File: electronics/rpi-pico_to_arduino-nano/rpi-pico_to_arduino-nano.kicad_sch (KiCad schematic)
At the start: 2 parts, among them U1 Pico

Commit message: add some connections and comments
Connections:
- net GPIO0: now reaches U1.1 (GPIO0)
- net GPIO0: now also A1.2 (D0/RX)
- net GPIO7: now reaches U1.10 (GPIO7)
- net GPIO7: now also A1.10 (D7)
- net GPIO8: now reaches U1.11 (GPIO8)
- net GPIO8: now also A1.11 (D8)
- net GPIO9: now reaches U1.12 (GPIO9)
- net GPIO9: now also A1.12 (D9)
- net GND: now reaches U1.13 (GND)
- net GND: now also A1.29 (GND), A1.4 (GND), U1.18 (GND), U1.23 (GND), U1.28 (GND), U1.3 (GND), U1.33 (AGND), U1.38 (GND), U1.42 (GND), U1.8 (GND)
- net GPIO10: now reaches U1.14 (GPIO10)
- net GPIO10: now also A1.13 (D10)
- net GPIO11: now reaches U1.15 (GPIO11)
- net GPIO11: now also A1.14 (D11)
- net GPIO12: now reaches U1.16 (GPIO12)
- net GPIO12: now also A1.15 (D12)
- net GPIO13: now reaches U1.17 (GPIO13)
- net GPIO13: now also A1.16 (D13)
- net GPIO14: now reaches U1.19 (GPIO14)
- net GPIO1: now reaches U1.2 (GPIO1)
- net GPIO1: now also A1.1 (D1/TX)
- net GPIO15: now reaches U1.20 (GPIO15)
- net GPIO16: now reaches U1.21 (GPIO16)
- net GPIO17: now reaches U1.22 (GPIO17)
- net GPIO18: now reaches U1.24 (GPIO18)
- net GPIO19: now reaches U1.25 (GPIO19)
- net GPIO20: now reaches U1.26 (GPIO20)
- net GPIO21: now reaches U1.27 (GPIO21)
- net GPIO22: now reaches U1.29 (GPIO22)
- net RUN: now reaches U1.30 (RUN)
- net GPIO26_ADC0: now reaches U1.31 (GPIO26_ADC0)
- net GPIO26_ADC0: now also A1.19 (A0), A1.21 (A2)
- net GPIO27_ADC1: now reaches U1.32 (GPIO27_ADC1)
- net GPIO27_ADC1: now also A1.20 (A1)
- net GPIO28_ADC2: now reaches U1.34 (GPIO28_ADC2)
- net ADC_VREF: now reaches U1.35 (ADC_VREF)
- net 3V3: now reaches U1.36 (3V3)
- net 3V3_EN: now reaches U1.37 (3V3_EN)
- net VSYS: now reaches U1.39 (VSYS)
- net GPIO2: now reaches U1.4 (GPIO2)
- net GPIO2: now also A1.5 (D2)
- net VBUS: now reaches U1.40 (VBUS)
- net SWCLK: now reaches U1.41 (SWCLK)
- net SWDIO: now reaches U1.43 (SWDIO)
- net GPIO3: now reaches U1.5 (GPIO3)
- net GPIO3: now also A1.6 (D3)
- net GPIO4: now reaches U1.6 (GPIO4)
- net GPIO4: now also A1.7 (D4)
- net GPIO5: now reaches U1.7 (GPIO5)
- net GPIO5: now also A1.8 (D5)
- net GPIO6: now reaches U1.9 (GPIO6)
- net GPIO6: now also A1.9 (D6)
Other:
- note added: "!!! TODO: check if connections at the Arduino make sense => also according to relay print!!!! => Pico Relay B will not work currently!!!! It should work out of the box (without modifications) !!!"
- note added: "Pico Relay B pinout"
- moved on the sheet: A1, U1

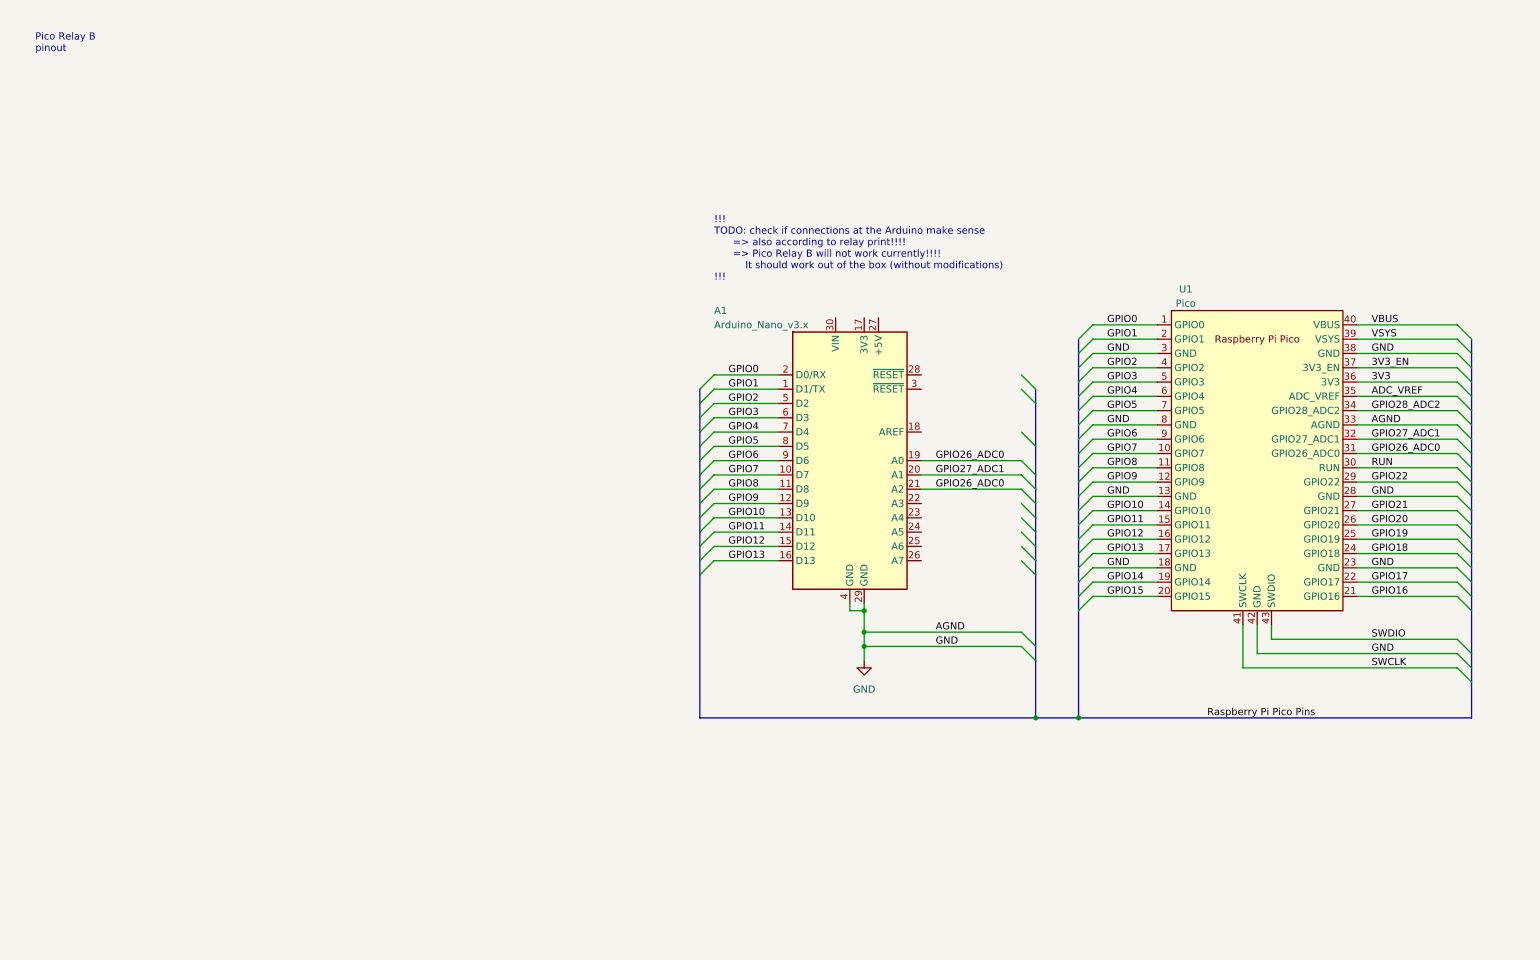
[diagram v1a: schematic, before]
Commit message: add connection matrix
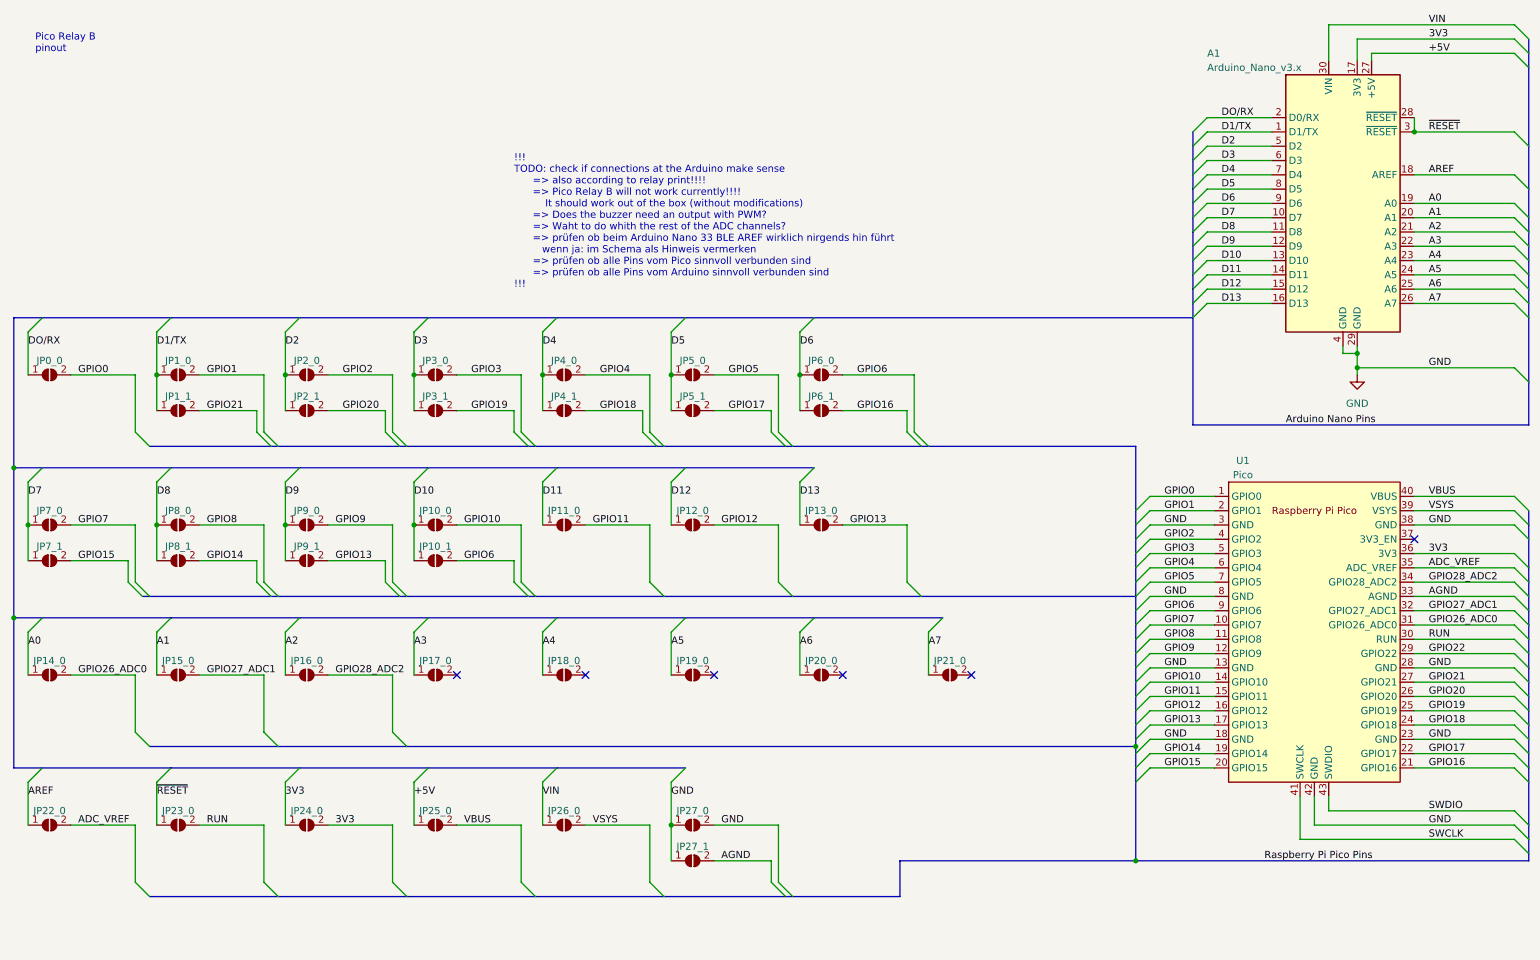
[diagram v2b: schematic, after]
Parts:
- added JP0_0, JP10_0, JP10_1, JP11_0, JP12_0, JP13_0, JP14_0, JP15_0, JP16_0, JP17_0, JP18_0, JP19_0, JP1_0, JP1_1, JP20_0, JP21_0, JP22_0, JP23_0, JP24_0, JP25_0, JP26_0, JP27_0, JP27_1, JP2_0, JP2_1, JP3_0, JP3_1, JP4_0, JP4_1, JP5_0, JP5_1, JP6_0, JP6_1, JP7_0, JP7_1, JP8_0, JP8_1, JP9_0, JP9_1: SolderJumper_2_Open, Jumper:SolderJumper-2_P1.3mm_Open_RoundedPad1.0x1.5mm, symbol Jumper:SolderJumper_2_Open
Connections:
- net 3V3: now also A1.17 (3V3), JP24_0.1 (A), JP24_0.2 (B)
- net ADC_VREF: now also JP22_0.2 (B)
- net GND: now also JP27_0.1 (A), JP27_0.2 (B), JP27_1.1 (A); no longer U1.33 (AGND)
- net GPIO0: now also JP0_0.2 (B); no longer A1.2 (D0/RX)
- net GPIO1: now also JP1_0.2 (B); no longer A1.1 (D1/TX)
- net GPIO10: now also JP10_0.2 (B); no longer A1.13 (D10)
- net GPIO11: now also JP11_0.2 (B); no longer A1.14 (D11)
- net GPIO12: now also JP12_0.2 (B); no longer A1.15 (D12)
- net GPIO13: now also JP13_0.2 (B), JP9_1.2 (B); no longer A1.16 (D13)
- net GPIO14: now also JP8_1.2 (B)
- net GPIO15: now also JP7_1.2 (B)
- net GPIO16: now also JP6_1.2 (B)
- net GPIO17: now also JP5_1.2 (B)
- net GPIO18: now also JP4_1.2 (B)
- net GPIO19: now also JP3_1.2 (B)
- net GPIO2: now also JP2_0.2 (B); no longer A1.5 (D2)
- net GPIO20: now also JP2_1.2 (B)
- net GPIO21: now also JP1_1.2 (B)
- net GPIO26_ADC0: now also JP14_0.2 (B); no longer A1.19 (A0), A1.21 (A2)
- net GPIO27_ADC1: now also JP15_0.2 (B); no longer A1.20 (A1)
- net GPIO28_ADC2: now also JP16_0.2 (B)
- net GPIO3: now also JP3_0.2 (B); no longer A1.6 (D3)
- net GPIO4: now also JP4_0.2 (B); no longer A1.7 (D4)
- net GPIO5: now also JP5_0.2 (B); no longer A1.8 (D5)
- net GPIO6: now also JP10_1.2 (B), JP6_0.2 (B); no longer A1.9 (D6)
- net GPIO7: now also JP7_0.2 (B); no longer A1.10 (D7)
- net GPIO8: now also JP8_0.2 (B); no longer A1.11 (D8)
- net GPIO9: now also JP9_0.2 (B); no longer A1.12 (D9)
- net RUN: now also JP23_0.2 (B)
- net VBUS: now also JP25_0.2 (B)
- net VSYS: now also JP26_0.2 (B)
- net AREF: now reaches A1.18 (AREF)
- net AREF: now also JP22_0.1 (A)
- net A3: now reaches A1.22 (A3)
- net A3: now also JP17_0.1 (A)
- net A4: now reaches A1.23 (A4)
- net A4: now also JP18_0.1 (A)
- net A5: now reaches A1.24 (A5)
- net A5: now also JP19_0.1 (A)
- net A6: now reaches A1.25 (A6)
- net A6: now also JP20_0.1 (A)
- net A7: now reaches A1.26 (A7)
- net A7: now also JP21_0.1 (A)
- net +5V: now reaches A1.27 (+5V)
- net +5V: now also JP25_0.1 (A)
- net ~{RESET}: now reaches A1.28 (~{RESET})
- net ~{RESET}: now also A1.3 (~{RESET}), JP23_0.1 (A)
- net VIN: now reaches A1.30 (VIN)
- net VIN: now also JP26_0.1 (A)
- net 3V3_EN: no longer names the net of U1.37 (3V3_EN)
- new net A0: A1.19 (A0), JP14_0.1 (A)
- new net A1: A1.20 (A1), JP15_0.1 (A)
- new net A2: A1.21 (A2), JP16_0.1 (A)
- new net AGND: JP27_1.2 (B), U1.33 (AGND)
- new net D10: A1.13 (D10), JP10_0.1 (A), JP10_1.1 (A)
- new net D11: A1.14 (D11), JP11_0.1 (A)
- new net D12: A1.15 (D12), JP12_0.1 (A)
- new net D13: A1.16 (D13), JP13_0.1 (A)
- new net D1/TX: A1.1 (D1/TX), JP1_0.1 (A), JP1_1.1 (A)
- new net D2: A1.5 (D2), JP2_0.1 (A), JP2_1.1 (A)
- new net D3: A1.6 (D3), JP3_0.1 (A), JP3_1.1 (A)
- new net D4: A1.7 (D4), JP4_0.1 (A), JP4_1.1 (A)
- new net D5: A1.8 (D5), JP5_0.1 (A), JP5_1.1 (A)
- new net D6: A1.9 (D6), JP6_0.1 (A), JP6_1.1 (A)
- new net D7: A1.10 (D7), JP7_0.1 (A), JP7_1.1 (A)
- new net D8: A1.11 (D8), JP8_0.1 (A), JP8_1.1 (A)
- new net D9: A1.12 (D9), JP9_0.1 (A), JP9_1.1 (A)
- new net DO/RX: A1.2 (D0/RX), JP0_0.1 (A)
- no-connect marks 0 -> 6
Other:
- note added: "!!! TODO: check if connections at the Arduino make sense => also according to relay print!!!! => Pico Relay B will not work currently!!!! It should work out of the box (without modifications) => Does the buzzer need an output with PWM? => Waht to do whith the rest of the ADC channels? => prüfen ob beim Arduino Nano 33 BLE AREF wirklich nirgends hin führt wenn ja: im Schema als Hinweis vermerken =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"
- note removed: "!!! TODO: check if connections at the Arduino make sense => also according to relay print!!!! => Pico Relay B will not work currently!!!! It should work out of the box (without modifications) !!!"
- moved on the sheet: A1, U1

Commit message: place components on pcb
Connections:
- net 3V3: no longer JP24_0.2 (B), U1.36 (3V3)
- net GND: no longer JP27_0.2 (B), U1.13 (GND), U1.18 (GND), U1.23 (GND), U1.28 (GND), U1.3 (GND), U1.38 (GND), U1.42 (GND), U1.8 (GND)
- net GPIO22: now also JP17_0.2 (B)
- net SWCLK: no longer names the net of U1.41 (SWCLK)
- net SWDIO: no longer names the net of U1.43 (SWDIO)
- new net 3V3_pico: JP24_0.2 (B), U1.36 (3V3)
- new net GND_pico: JP27_0.2 (B), U1.13 (GND), U1.18 (GND), U1.23 (GND), U1.28 (GND), U1.3 (GND), U1.38 (GND), U1.42 (GND), U1.8 (GND)
- no-connect marks 6 -> 7
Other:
- note added: "!!! TODO: check if connections at the Arduino make sense (done)=> Does the buzzer need an output with PWM? => yes and done => how does the rgb led work and with only one pin? => prüfen ob beim Arduino Nano 33 BLE AREF wirklich nirgends hin führt wenn ja: im Schema als Hinweis vermerken => entscheiden welche Lötjumper per default geschlossen sein sollen !!! Delete this text before when done"
- note removed: "!!! TODO: check if connections at the Arduino make sense => also according to relay print!!!! => Pico Relay B will not work currently!!!! It should work out of the box (without modifications) => Does the buzzer need an output with PWM? => Waht to do whith the rest of the ADC channels? => prüfen ob beim Arduino Nano 33 BLE AREF wirklich nirgends hin führt wenn ja: im Schema als Hinweis vermerken =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"
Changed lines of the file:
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@@
   (junction (at 16.51 104.14) (diameter 0) (color 0 0 0 0)
   )
+  (no_connect (at 262.89 106.68))
+  (no_connect (at 247.65 152.4))
+  (no_connect (at 242.57 152.4))
   (no_connect (at 184.15 130.81))
   (no_connect (at 161.29 130.81))
-  (no_connect (at 115.57 130.81))
-  (no_connect (at 92.71 130.81))
   (no_connect (at 138.43 130.81))
-  (no_connect (at 262.89 106.68))
+  (no_connect (at 115.57 130.81))
   (bus_entry (at 80.01 114.3) (size 2.54 2.54)
     (stroke (width 0) (type default) (color 0 0 0 0))
@@
     (stroke (width 0) (type default) (color 0 0 0 0))
   )
+  (bus_entry (at 104.14 140.97) (size 2.54 2.54)
+    (stroke (width 0) (type default) (color 0 0 0 0))
+  )
   (bus_entry (at 87.63 147.32) (size -2.54 2.54)
     (stroke (width 0) (type default) (color 0 0 0 0))
@@
     (stroke (width 0) (type default) (color 0 0 0 0))
   )
-  (bus_entry (at 283.21 157.48) (size -2.54 -2.54)
-    (stroke (width 0) (type default) (color 0 0 0 0))
-  )
-  (bus_entry (at 280.67 160.02) (size 2.54 2.54)
-    (stroke (width 0) (type default) (color 0 0 0 0))
-  )
   (bus_entry (at 133.35 67.31) (size -2.54 2.54)
     (stroke (width 0) (type default) (color 0 0 0 0))
@@
     (stroke (width 0) (type default) (color 0 0 0 0))
   )
-  (wire (pts (xy 242.57 152.4) (xy 242.57 160.02))
-    (stroke (width 0) (type default) (color 0 0 0 0))
-  )
   (wire (pts (xy 215.9 111.76) (xy 227.33 111.76))
     (stroke (width 0) (type default) (color 0 0 0 0))
@@
     (stroke (width 0) (type default) (color 0 0 0 0))
   )
-  (bus (pts (xy 283.21 162.56) (xy 283.21 163.83))
+  (bus (pts (xy 283.21 160.02) (xy 283.21 163.83))
     (stroke (width 0) (type default) (color 0 0 0 0))
   )
@@
     (stroke (width 0) (type default) (color 0 0 0 0))
   )
-  (bus (pts (xy 283.21 149.86) (xy 283.21 157.48))
+  (bus (pts (xy 283.21 149.86) (xy 283.21 160.02))
     (stroke (width 0) (type default) (color 0 0 0 0))
   )
@@
     (stroke (width 0) (type default) (color 0 0 0 0))
   )
+  (wire (pts (xy 104.14 130.81) (xy 104.14 140.97))
+    (stroke (width 0) (type default) (color 0 0 0 0))
+  )
   (wire (pts (xy 92.71 157.48) (xy 104.14 157.48))
     (stroke (width 0) (type default) (color 0 0 0 0))
@@
     (stroke (width 0) (type default) (color 0 0 0 0))
   )
-  (wire (pts (xy 247.65 152.4) (xy 247.65 154.94))
-    (stroke (width 0) (type default) (color 0 0 0 0))
-  )
   (wire (pts (xy 262.89 121.92) (xy 280.67 121.92))
     (stroke (width 0) (type default) (color 0 0 0 0))
@@
     (stroke (width 0) (type default) (color 0 0 0 0))
   )
+  (bus (pts (xy 106.68 143.51) (xy 213.36 143.51))
+    (stroke (width 0) (type default) (color 0 0 0 0))
+  )
   (bus (pts (xy 213.36 119.38) (xy 213.36 121.92))
     (stroke (width 0) (type default) (color 0 0 0 0))
@@
     (stroke (width 0) (type default) (color 0 0 0 0))
   )
+  (wire (pts (xy 92.71 130.81) (xy 104.14 130.81))
+    (stroke (width 0) (type default) (color 0 0 0 0))
+  )
   (wire (pts (xy 58.42 77.47) (xy 58.42 87.63))
     (stroke (width 0) (type default) (color 0 0 0 0))
@@
     (stroke (width 0) (type default) (color 0 0 0 0))
   )
-  (bus (pts (xy 283.21 157.48) (xy 283.21 160.02))
-    (stroke (width 0) (type default) (color 0 0 0 0))
-  )
   (wire (pts (xy 226.06 34.29) (xy 237.49 34.29))
     (stroke (width 0) (type default) (color 0 0 0 0))
@@
     (stroke (width 0) (type default) (color 0 0 0 0))
   )
-  (bus (pts (xy 83.82 143.51) (xy 213.36 143.51))
+  (bus (pts (xy 83.82 143.51) (xy 106.68 143.51))
     (stroke (width 0) (type default) (color 0 0 0 0))
   )
@@
     (stroke (width 0) (type default) (color 0 0 0 0))
   )
-  (wire (pts (xy 247.65 154.94) (xy 280.67 154.94))
-    (stroke (width 0) (type default) (color 0 0 0 0))
-  )
   (wire (pts (xy 16.51 69.85) (xy 16.51 77.47))
     (stroke (width 0) (type default) (color 0 0 0 0))
@@
     (stroke (width 0) (type default) (color 0 0 0 0))
   )
-  (wire (pts (xy 242.57 160.02) (xy 280.67 160.02))
-    (stroke (width 0) (type default) (color 0 0 0 0))
-  )
   (wire (pts (xy 24.13 77.47) (xy 35.56 77.47))
     (stroke (width 0) (type default) (color 0 0 0 0))
@@
     (stroke (width 0) (type default) (color 0 0 0 0))
   )
-  (bus (pts (xy 283.21 160.02) (xy 283.21 162.56))
-    (stroke (width 0) (type default) (color 0 0 0 0))
-  )
   (wire (pts (xy 247.65 15.24) (xy 247.65 21.59))
     (stroke (width 0) (type default) (color 0 0 0 0))
@@
     )
   )
-  (text "!!!\nTODO: check if connections at the Arduino make sense\n      => also according to relay print!!!!\n      => Pico Relay B will not work currently!!!!\n          It should work out of the box (without modifications)\n      => Does the buzzer need an output with PWM?\n      => Waht to do whith the rest of the ADC channels?\n      => prüfen ob beim Arduino Nano 33 BLE AREF wirklich nirgends hin führt\n         wenn ja: im Schema als Hinweis vermerken\n      => prüfen ob alle Pins vom Pico sinnvoll verbunden sind\n      => prüfen ob alle Pins vom Arduino sinnvoll verbunden sind\n!!!"
+  (text "!!!\nTODO: check if connections at the Arduino make sense\n      (done)=> Does the buzzer need an output with PWM? => yes and done\n      => how does the rgb led work and with only one pin?\n      => prüfen ob beim Arduino Nano 33 BLE AREF wirklich nirgends hin führt\n         wenn ja: im Schema als Hinweis vermerken\n      => entscheiden welche Lötjumper per default geschlossen sein sollen\n!!!\n\nDelete this text before when done"
     (at 102.87 62.23 0)
     (effects (font (size 1.27 1.27)) (justify left bottom))
@@
     (effects (font (size 1.27 1.27)) (justify left bottom))
   )
-  (label "GND" (at 218.44 116.84 0)
+  (label "GPIO22" (at 93.98 130.81 0)
+    (effects (font (size 1.27 1.27)) (justify left bottom))
+  )
+  (label "GND_pico" (at 218.44 116.84 0)
     (effects (font (size 1.27 1.27)) (justify left bottom))
   )
@@
     (effects (font (size 1.27 1.27)) (justify left bottom))
   )
-  (label "GND" (at 265.43 129.54 0)
+  (label "GND_pico" (at 265.43 129.54 0)
     (effects (font (size 1.27 1.27)) (justify left bottom))
   )
@@
     (effects (font (size 1.27 1.27)) (justify left bottom))
   )
-  (label "GND" (at 265.43 142.24 0)
+  (label "GND_pico" (at 265.43 142.24 0)
     (effects (font (size 1.27 1.27)) (justify left bottom))
   )
@@
     (effects (font (size 1.27 1.27)) (justify left bottom))
   )
-  (label "GND" (at 218.44 129.54 0)
+  (label "GND_pico" (at 218.44 129.54 0)
     (effects (font (size 1.27 1.27)) (justify left bottom))
   )
@@
     (effects (font (size 1.27 1.27)) (justify left bottom))
   )
-  (label "3V3" (at 265.43 109.22 0)
+  (label "3V3_pico" (at 265.43 109.22 0)
     (effects (font (size 1.27 1.27)) (justify left bottom))
   )
@@
     (effects (font (size 1.27 1.27)) (justify left bottom))
   )
-  (label "GND" (at 139.7 157.48 0)
+  (label "GND_pico" (at 139.7 157.48 0)
     (effects (font (size 1.27 1.27)) (justify left bottom))
   )
@@
     (effects (font (size 1.27 1.27)) (justify left bottom))
   )
-  (label "GND" (at 265.43 157.48 0)
+  (label "GND_pico" (at 265.43 157.48 0)
     (effects (font (size 1.27 1.27)) (justify left bottom))
   )
@@
     (effects (font (size 1.27 1.27)) (justify left bottom))
   )
-  (label "SWCLK" (at 265.43 160.02 0)
-    (effects (font (size 1.27 1.27)) (justify left bottom))
-  )
-  (label "3V3" (at 71.12 157.48 0)
+  (label "3V3_pico" (at 71.12 157.48 0)
     (effects (font (size 1.27 1.27)) (justify left bottom))
   )
@@
     (effects (font (size 1.27 1.27)) (justify left bottom))
   )
-  (label "SWDIO" (at 265.43 154.94 0)
-    (effects (font (size 1.27 1.27)) (justify left bottom))
-  )
   (label "D8" (at 228.6 52.07 0)
     (effects (font (size 1.27 1.27)) (justify left bottom))
@@
     (effects (font (size 1.27 1.27)) (justify left bottom))
   )
-  (label "GND" (at 265.43 104.14 0)
+  (label "GND_pico" (at 265.43 104.14 0)
     (effects (font (size 1.27 1.27)) (justify left bottom))
   )
@@
     (effects (font (size 1.27 1.27)) (justify left bottom))
   )
-  (label "GND" (at 218.44 104.14 0)
+  (label "GND_pico" (at 218.44 104.14 0)
     (effects (font (size 1.27 1.27)) (justify left bottom))
   )
@@
     (effects (font (size 1.27 1.27)) (justify left bottom))
   )
-  (label "GND" (at 218.44 142.24 0)
+  (label "GND_pico" (at 218.44 142.24 0)
     (effects (font (size 1.27 1.27)) (justify left bottom))
   )
